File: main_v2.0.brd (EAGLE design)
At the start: 49.5 x 25.7 mm, 74 parts, among them IC1 LM321MF, IC2 LM321MF, IC4 LM321MF, U1 BSC076N, U10 IR2101S, U11 TLV73333PDBVT, U2 STM32F030K6T6TR, U3 BSC076N, U4 BSC076N, U5 BSC076N, U6 IR2101S, U7 BSC076N, U8 IR2101S, U9 BSC076N, Y1 8MHz

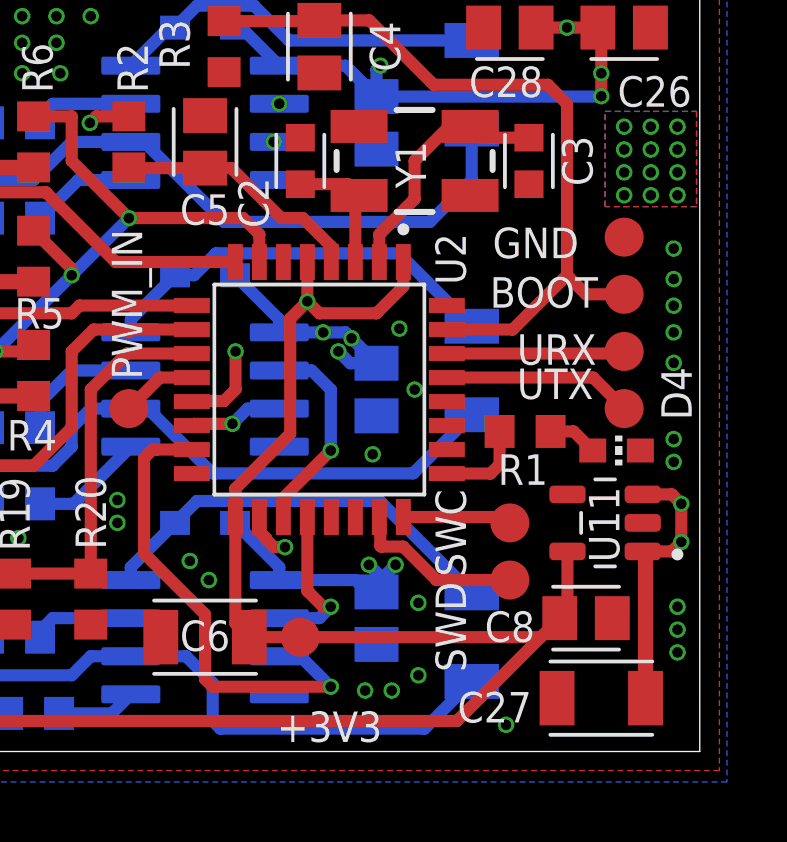
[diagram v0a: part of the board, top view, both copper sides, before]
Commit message: updated ldo regulator
we are tested working project
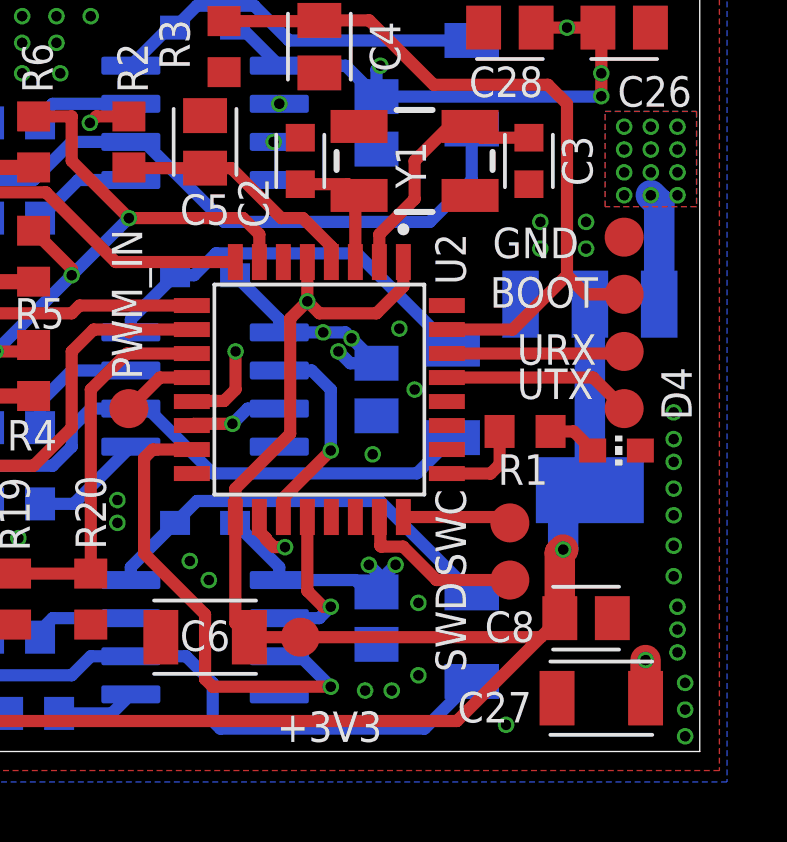
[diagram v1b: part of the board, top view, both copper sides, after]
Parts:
- U11: value TLV73333PDBVT -> (none); device TLV73333PDBVT:SOT95P280X145-5N -> SparkFun-IC-Power:SOT223
- moved U11 4.22 mm to (45.8, 86.1), flipped to the bottom
- moved C18 0.99 mm to (41.3, 86.2)
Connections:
- net +12V: no longer U11.1
- net +3.3V: now also U11.2, U11.4; no longer U11.5
- net GND: now also U11.1; no longer U11.2
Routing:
- net +3.3V: track 97.8 -> 106.7 mm, vias 5 -> 6
- net +12V: track 68.1 -> 64.1 mm, vias 74 -> 73
- net PHB: track 26.8 -> 25.9 mm
- net GND: vias 57 -> 64
